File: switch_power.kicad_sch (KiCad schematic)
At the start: 32 parts

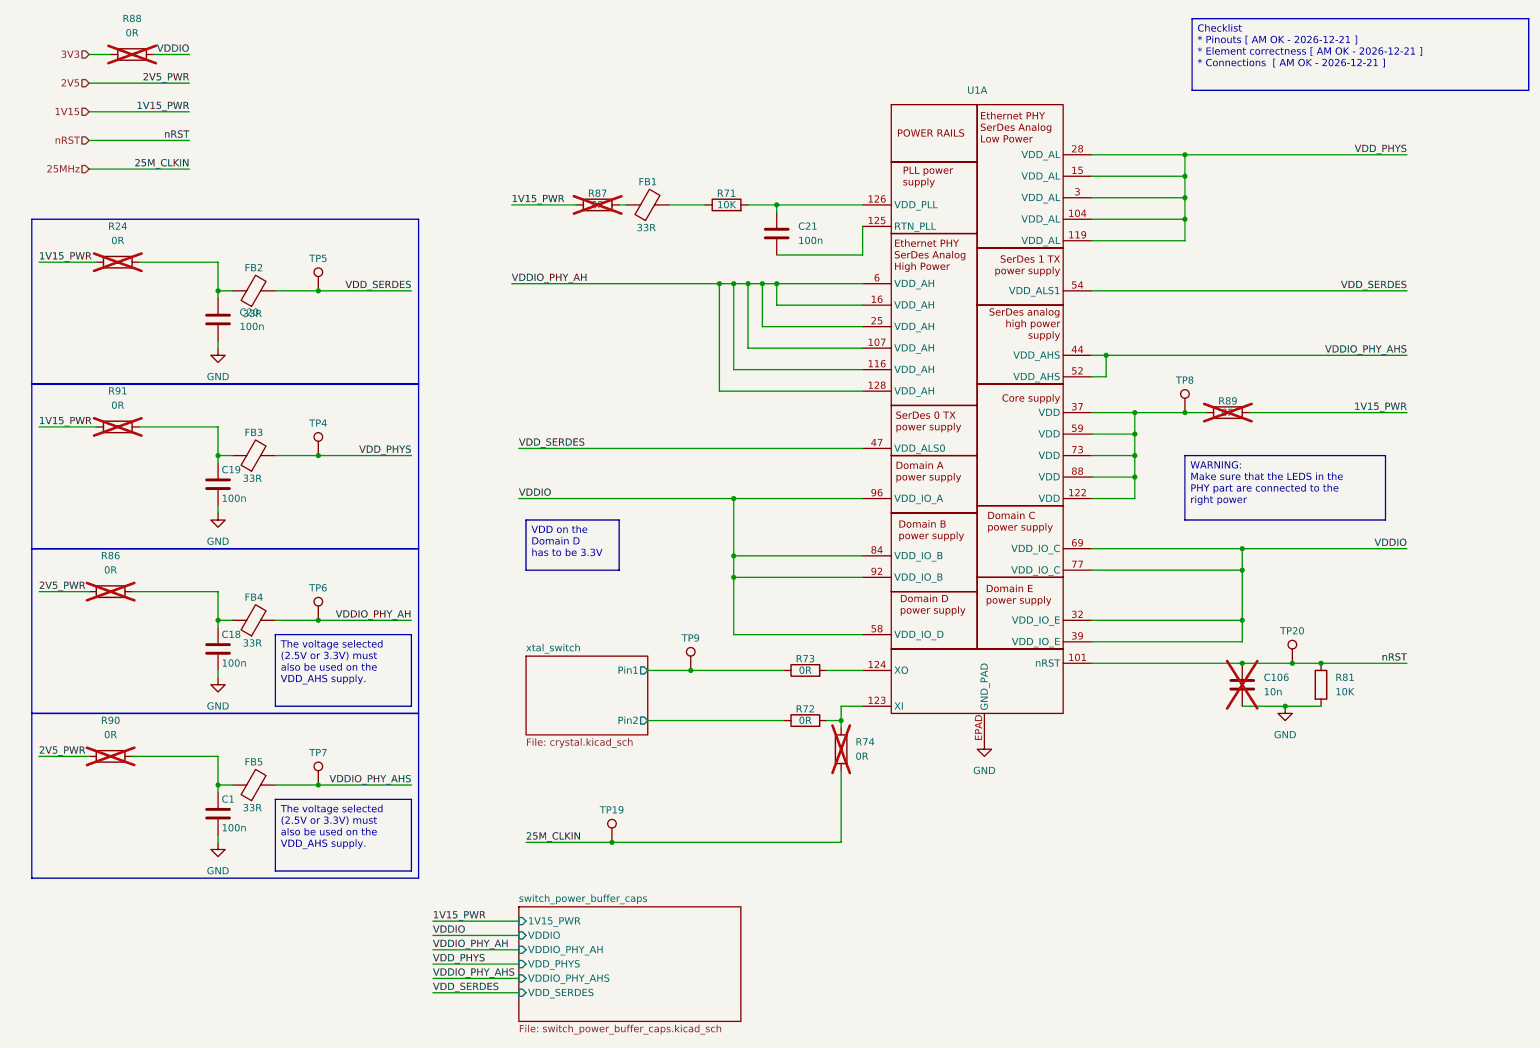
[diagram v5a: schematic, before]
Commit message: removes unused busses, adds cheaper 0R resistor, clean up to fix ERC errors. Refs: #1
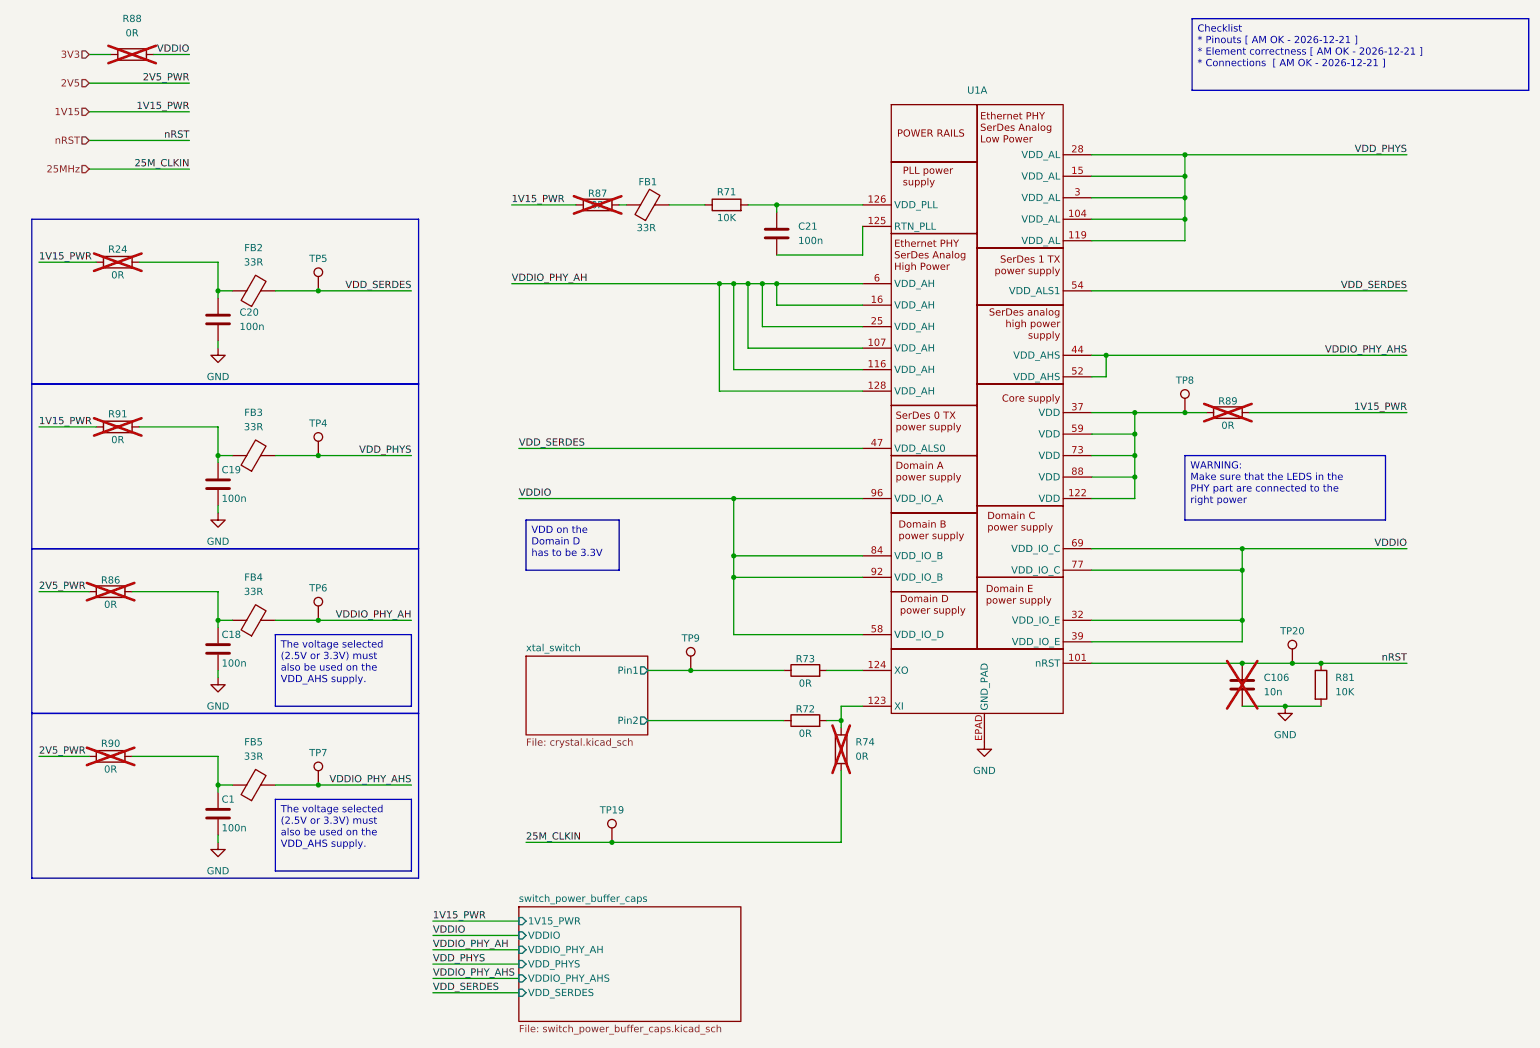
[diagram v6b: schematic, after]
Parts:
- R72, R73, R74: symbol KL_R:R_0R_250mW_0.5_0603 -> KL_R:R_0R_100mW_5_0603; Digikey 541-2779-1-ND -> YAG1307CT-ND; Farnell 3235077 -> (none); LCSC C2126552 -> C3017805; Mouser 71-RCS06030000Z0EA -> 603-RC0603JR-070RP; Power 250mW -> 0.1; Tolerance 0.5% -> 5
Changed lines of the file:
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@@
 		(on_board yes)
 		(dnp yes)
-		(fields_autoplaced yes)
 		(property "Reference" "R90"
-			(at 31.75 138.43 90)
+			(at 31.75 142.494 90)
 			(effects
 				(font
@@
 		)
 		(property "Value" "0R"
-			(at 31.75 140.97 90)
+			(at 31.75 147.066 90)
 			(effects
 				(font
@@
 		(dnp no)
 		(property "Reference" "R71"
-			(at 140.97 44.958 90)
+			(at 140.97 44.704 90)
 			(effects
 				(font
@@
 		)
 		(property "Value" "10K"
-			(at 140.97 46.99 90)
+			(at 140.97 49.276 90)
 			(effects
 				(font
@@
 		(on_board yes)
 		(dnp no)
+		(fields_autoplaced yes)
 		(property "Reference" "FB5"
-			(at 57.15 145.796 0)
+			(at 57.0992 142.24 0)
 			(effects
 				(font
@@
 		)
 		(property "Value" "33R"
-			(at 56.896 153.924 0)
+			(at 57.0992 144.78 0)
 			(effects
 				(font
@@
 		(on_board yes)
 		(dnp yes)
-		(fields_autoplaced yes)
 		(property "Reference" "R91"
-			(at 33.02 80.01 90)
+			(at 33.02 84.074 90)
 			(effects
 				(font
@@
 		)
 		(property "Value" "0R"
-			(at 33.02 82.55 90)
+			(at 33.02 88.646 90)
 			(effects
 				(font
@@
 	)
 	(symbol
-		(lib_id "KL_R:R_0R_250mW_0.5_0603")
+		(lib_id "KL_R:R_0R_100mW_5_0603")
 		(at 154.94 129.54 90)
 		(unit 1)
@@
 		)
 		(property "Value" "0R"
-			(at 154.94 129.54 90)
+			(at 154.94 131.826 90)
 			(effects
 				(font
@@
 			)
 		)
-		(property "Datasheet" "~"
+		(property "Datasheet" "https://yageogroup.com/component-documentation/download/specsheet/RC0603JR-070RP"
 			(at 154.94 129.54 0)
 			(effects
@@
 			)
 		)
-		(property "Power" "250mW"
+		(property "Power" "0.1"
 			(at 154.94 129.54 0)
 			(effects
@@
 			)
 		)
-		(property "Tolerance" "0.5%"
+		(property "Tolerance" "5"
 			(at 154.94 129.54 0)
 			(effects
@@
 			)
 		)
-		(property "Mouser" "71-RCS06030000Z0EA"
+		(property "Mouser" "603-RC0603JR-070RP"
 			(at 154.94 129.54 0)
 			(effects
@@
 			)
 		)
-		(property "Digikey" "541-2779-1-ND"
+		(property "Digikey" "YAG1307CT-ND"
 			(at 154.94 129.54 0)
 			(effects
@@
 			)
 		)
-		(property "LCSC" "C2126552"
+		(property "LCSC" "C3017805"
 			(at 154.94 129.54 0)
 			(effects
@@
 			)
 		)
-		(property "Farnell" "3235077"
+		(property "Farnell" ""
 			(at 154.94 129.54 0)
 			(effects
@@
 		(on_board yes)
 		(dnp yes)
-		(fields_autoplaced yes)
 		(property "Reference" "R24"
-			(at 33.02 50.8 90)
+			(at 33.02 54.864 90)
 			(effects
 				(font
@@
 		)
 		(property "Value" "0R"
-			(at 33.02 53.34 90)
+			(at 33.02 59.436 90)
 			(effects
 				(font
@@
 		(on_board yes)
 		(dnp no)
+		(fields_autoplaced yes)
 		(property "Reference" "FB3"
-			(at 57.15 87.376 0)
+			(at 57.0992 83.82 0)
 			(effects
 				(font
@@
 		)
 		(property "Value" "33R"
-			(at 56.896 95.504 0)
+			(at 57.0992 86.36 0)
 			(effects
 				(font
@@
 		)
 		(property "Value" "0R"
-			(at 229.87 83.82 90)
+			(at 229.87 86.106 90)
 			(effects
 				(font
@@
 	)
 	(symbol
-		(lib_id "KL_R:R_0R_250mW_0.5_0603")
+		(lib_id "KL_R:R_0R_100mW_5_0603")
 		(at 154.94 138.43 90)
 		(unit 1)
@@
 		)
 		(property "Value" "0R"
-			(at 154.94 138.43 90)
+			(at 154.94 140.716 90)
 			(effects
 				(font
@@
 			)
 		)
-		(property "Datasheet" "~"
+		(property "Datasheet" "https://yageogroup.com/component-documentation/download/specsheet/RC0603JR-070RP"
 			(at 154.94 138.43 0)
 			(effects
@@
 			)
 		)
-		(property "Power" "250mW"
+		(property "Power" "0.1"
 			(at 154.94 138.43 0)
 			(effects
@@
 			)
 		)
-		(property "Tolerance" "0.5%"
+		(property "Tolerance" "5"
 			(at 154.94 138.43 0)
 			(effects
@@
 			)
 		)
-		(property "Mouser" "71-RCS06030000Z0EA"
+		(property "Mouser" "603-RC0603JR-070RP"
 			(at 154.94 138.43 0)
 			(effects
@@
 			)
 		)
-		(property "Digikey" "541-2779-1-ND"
+		(property "Digikey" "YAG1307CT-ND"
 			(at 154.94 138.43 0)
 			(effects
@@
 			)
 		)
-		(property "LCSC" "C2126552"
+		(property "LCSC" "C3017805"
 			(at 154.94 138.43 0)
 			(effects
@@
 			)
 		)
-		(property "Farnell" "3235077"
+		(property "Farnell" ""
 			(at 154.94 138.43 0)
 			(effects
@@
 		(on_board yes)
 		(dnp yes)
-		(fields_autoplaced yes)
 		(property "Reference" "R86"
-			(at 31.75 109.22 90)
+			(at 31.75 113.538 90)
 			(effects
 				(font
@@
 		)
 		(property "Value" "0R"
-			(at 31.75 111.76 90)
+			(at 31.75 117.856 90)
 			(effects
 				(font
@@
 		(on_board yes)
 		(dnp no)
+		(fields_autoplaced yes)
 		(property "Reference" "FB4"
-			(at 57.15 116.586 0)
+			(at 57.0992 113.03 0)
 			(effects
 				(font
@@
 		)
 		(property "Value" "33R"
-			(at 56.896 124.714 0)
+			(at 57.0992 115.57 0)
 			(effects
 				(font
@@
 	)
 	(symbol
-		(lib_id "KL_R:R_0R_250mW_0.5_0603")
+		(lib_id "KL_R:R_0R_100mW_5_0603")
 		(at 161.29 143.51 180)
 		(unit 1)
@@
 			)
 		)
-		(property "Datasheet" "~"
+		(property "Datasheet" "https://yageogroup.com/component-documentation/download/specsheet/RC0603JR-070RP"
 			(at 161.29 143.51 0)
 			(effects
@@
 			)
 		)
-		(property "Power" "250mW"
+		(property "Power" "0.1"
 			(at 161.29 143.51 0)
 			(effects
@@
 			)
 		)
-		(property "Tolerance" "0.5%"
+		(property "Tolerance" "5"
 			(at 161.29 143.51 0)
 			(effects
@@
 			)
 		)
-		(property "Mouser" "71-RCS06030000Z0EA"
+		(property "Mouser" "603-RC0603JR-070RP"
 			(at 161.29 143.51 0)
 			(effects
@@
 			)
 		)
-		(property "Digikey" "541-2779-1-ND"
+		(property "Digikey" "YAG1307CT-ND"
 			(at 161.29 143.51 0)
 			(effects
@@
 			)
 		)
-		(property "LCSC" "C2126552"
+		(property "LCSC" "C3017805"
 			(at 161.29 143.51 0)
 			(effects
@@
 			)
 		)
-		(property "Farnell" "3235077"
+		(property "Farnell" ""
 			(at 161.29 143.51 0)
 			(effects
@@
 		(on_board yes)
 		(dnp no)
+		(fields_autoplaced yes)
 		(property "Reference" "FB2"
-			(at 57.15 58.166 0)
+			(at 57.0992 54.61 0)
 			(effects
 				(font
@@
 		)
 		(property "Value" "33R"
-			(at 56.896 66.294 0)
+			(at 57.0992 57.15 0)
 			(effects
 				(font

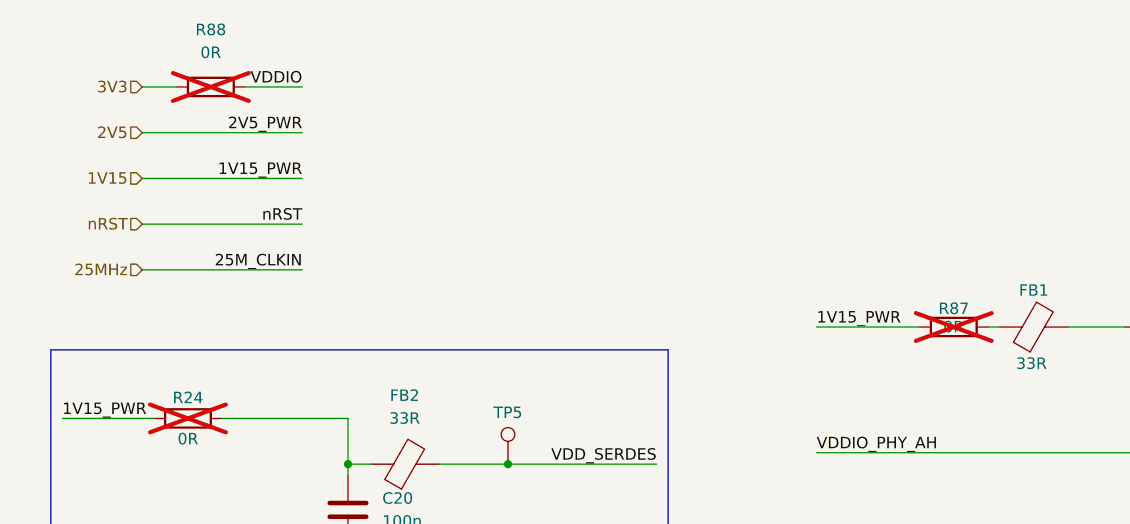
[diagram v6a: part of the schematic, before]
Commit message: consistent naming for hierarchical pin and attached net. Refs: #1
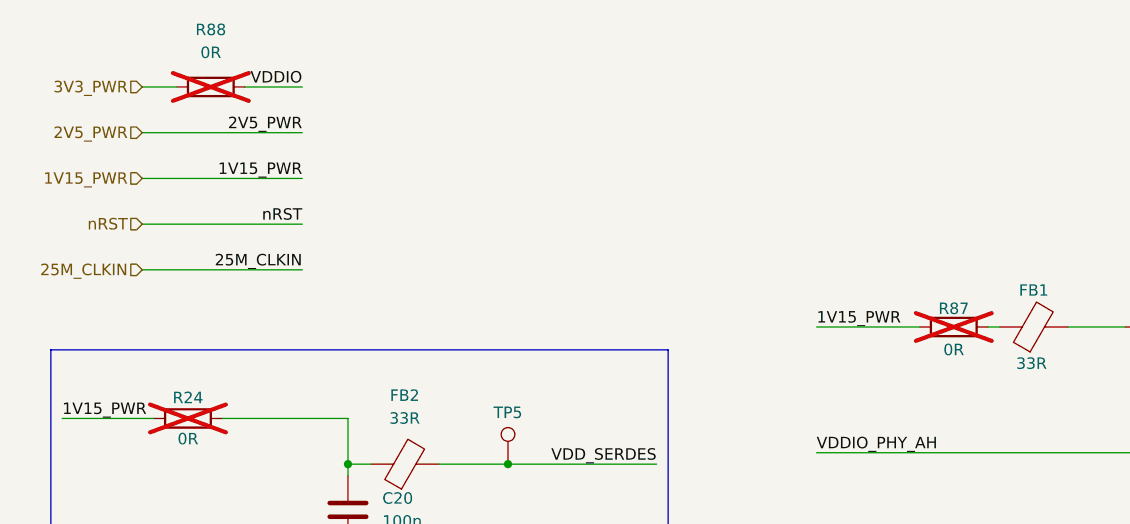
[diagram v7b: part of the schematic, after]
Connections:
- net 1V15 renamed 1V15_PWR
- net 25MHz renamed 25M_CLKIN
- net 2V5 renamed 2V5_PWR
- net 3V3 renamed 3V3_PWR
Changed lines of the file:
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@@
 		)
 	)
-	(hierarchical_label "25MHz"
+	(hierarchical_label "25M_CLKIN"
 		(shape input)
 		(at 27.94 40.64 180)
@@
 		)
 	)
-	(hierarchical_label "2V5"
+	(hierarchical_label "2V5_PWR"
 		(shape input)
 		(at 27.94 25.4 180)
@@
 		)
 	)
-	(hierarchical_label "1V15"
+	(hierarchical_label "1V15_PWR"
 		(shape input)
 		(at 27.94 30.48 180)
@@
 		)
 	)
-	(hierarchical_label "3V3"
+	(hierarchical_label "3V3_PWR"
 		(shape input)
 		(at 27.94 20.32 180)
@@
 		)
 		(property "Value" "0R"
-			(at 118.11 46.99 90)
+			(at 118.11 49.53 90)
 			(effects
 				(font
